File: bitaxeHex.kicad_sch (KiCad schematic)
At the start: 26 parts, among them J1 Screw Terminal, J2 Screw Terminal

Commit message: minor update
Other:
- sheet BM1366-1 renamed BM1368-1
- sheet BM1366-2 renamed BM1368-2
- sheet BM1366-3 renamed BM1368-3
- sheet ESP32 ports: added 1V2_IO; removed 1V8_IO
- sheet Power ports: added 1V2_IO; removed 1V8_IO
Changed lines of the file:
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@@
 		)
 	)
-	(label "1V8"
+	(label "1V2"
 		(at 50.165 88.265 0)
 		(fields_autoplaced yes)
@@
 		)
 	)
-	(label "1V8"
+	(label "1V2"
 		(at 86.995 36.195 180)
 		(fields_autoplaced yes)
@@
 			(color 255 255 194 1.0000)
 		)
-		(property "Sheetname" "BM1366-1"
+		(property "Sheetname" "BM1368-1"
 			(at 127.635 73.66 0)
 			(effects
@@
 			(color 255 255 194 1.0000)
 		)
-		(property "Sheetname" "BM1366-2"
+		(property "Sheetname" "BM1368-2"
 			(at 165.1 73.66 0)
 			(effects
@@
 			)
 		)
-		(pin "1V8_IO" output
+		(pin "1V2_IO" output
 			(at 79.375 36.195 0)
 			(effects
@@
 			)
 		)
-		(pin "1V8_IO" input
+		(pin "1V2_IO" input
 			(at 59.69 88.265 180)
 			(effects
@@
 			(color 255 255 194 1.0000)
 		)
-		(property "Sheetname" "BM1366-3"
+		(property "Sheetname" "BM1368-3"
 			(at 203.835 73.66 0)
 			(effects

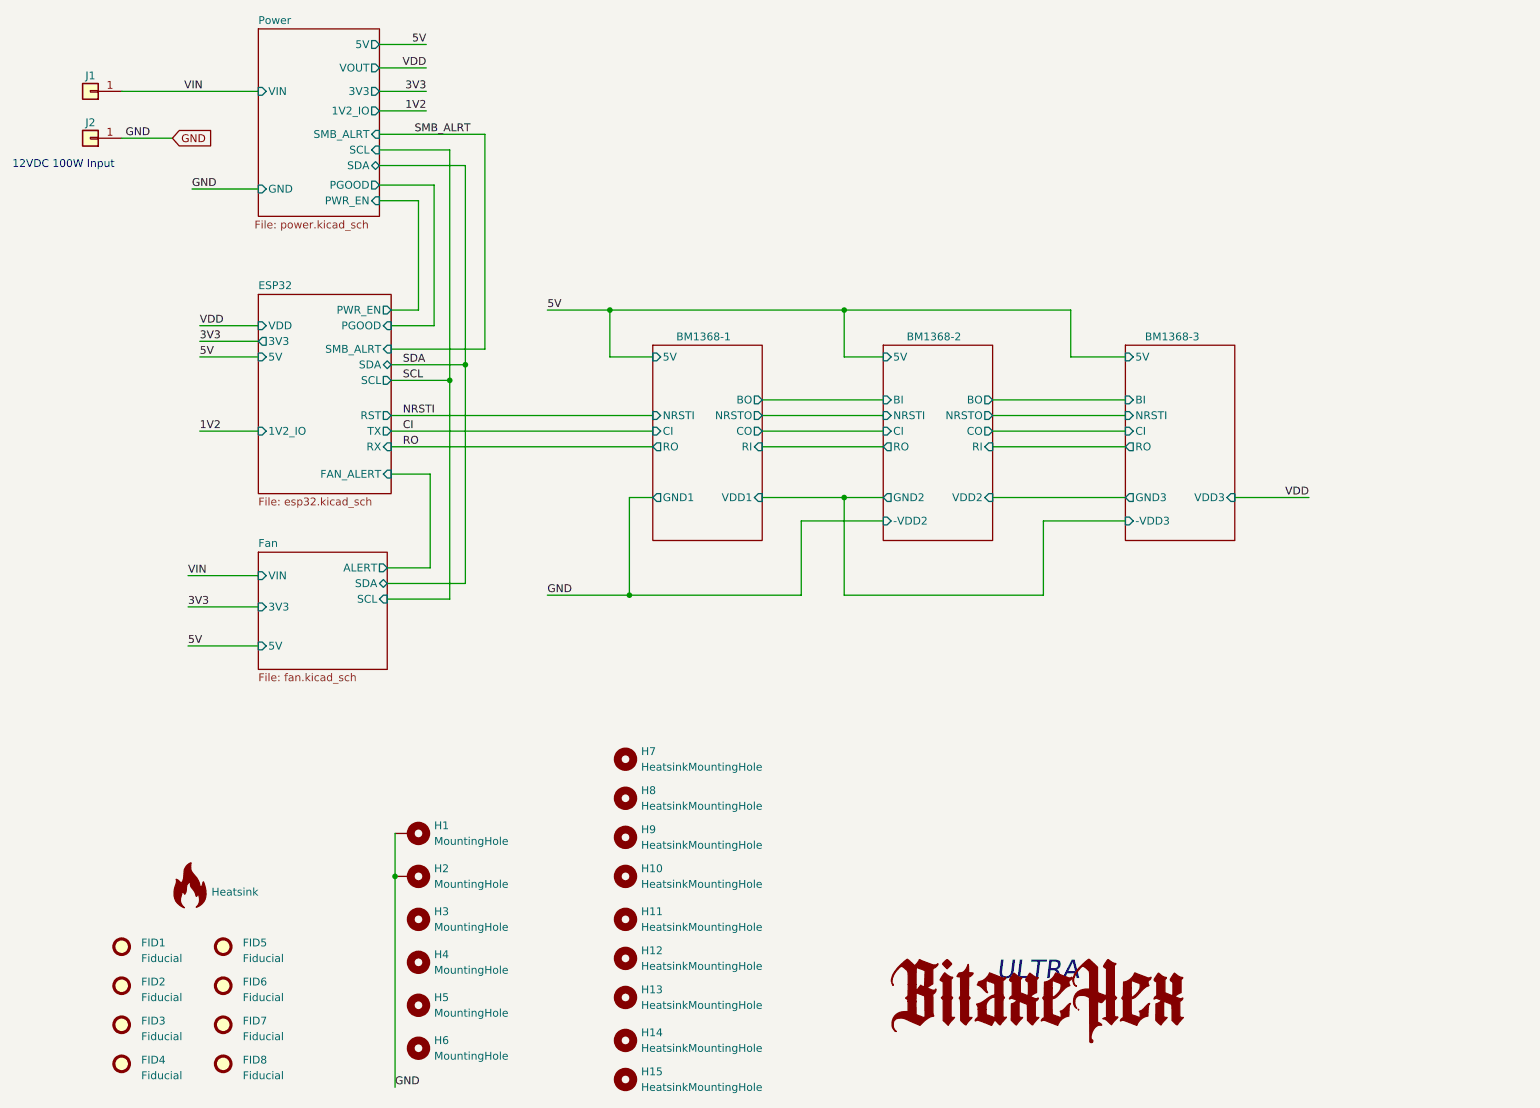
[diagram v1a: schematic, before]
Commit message: Adding temperature monitoring
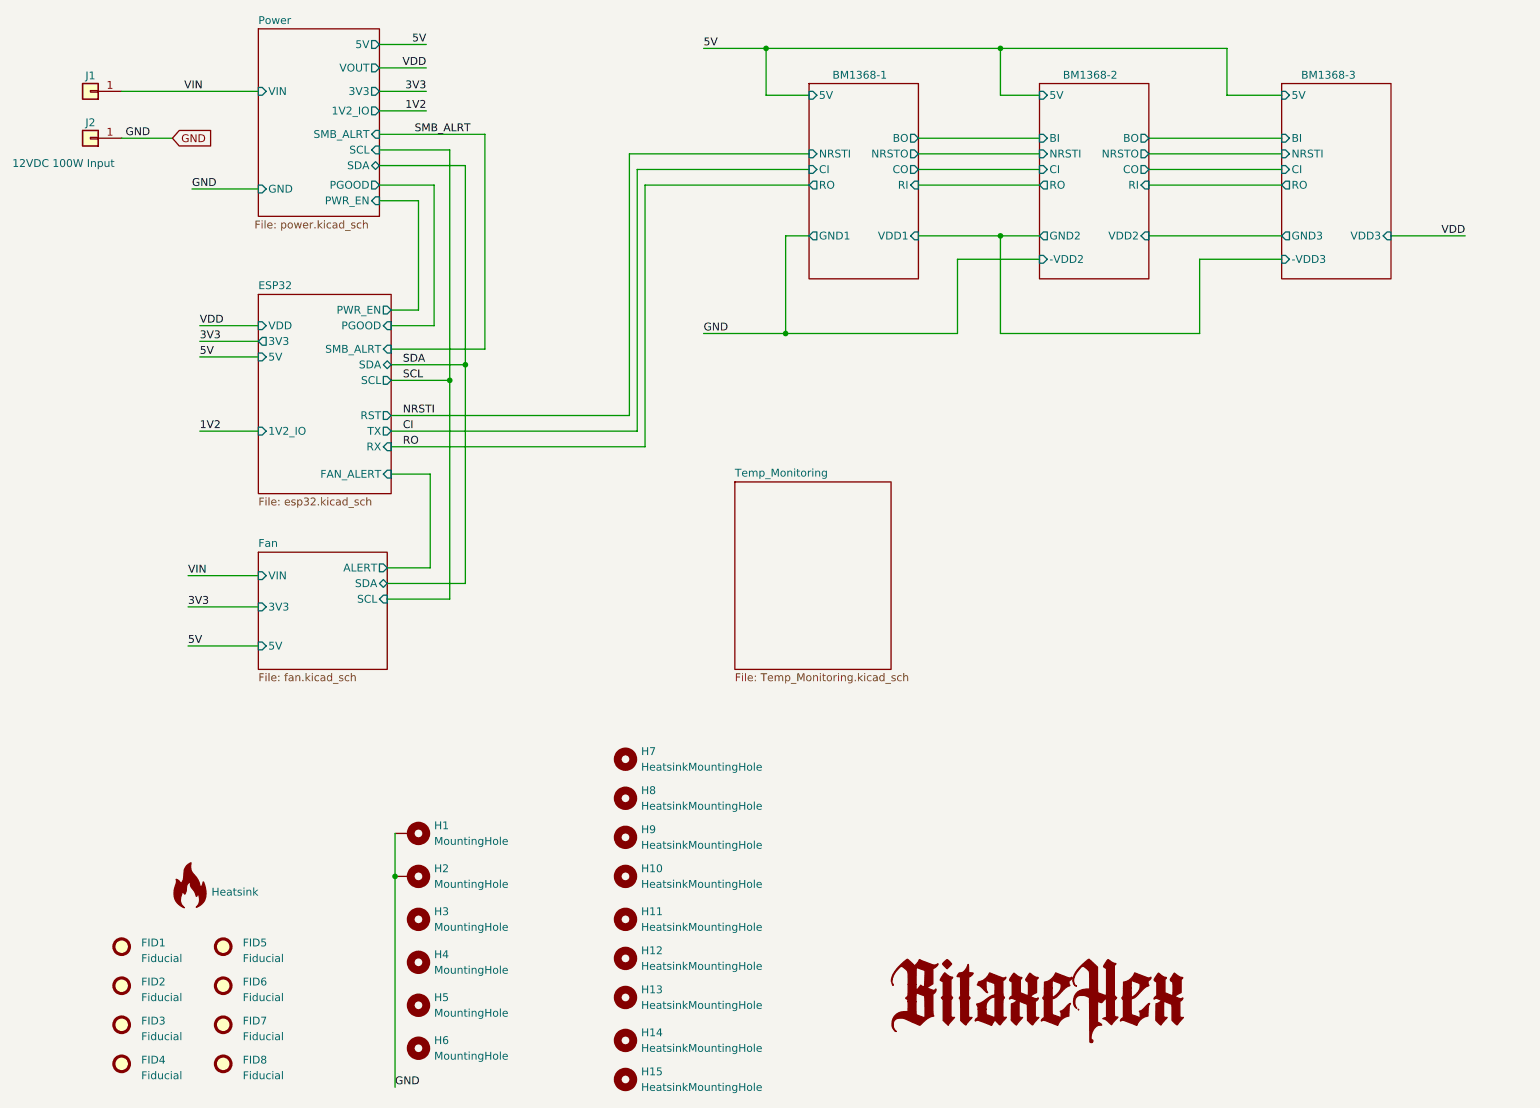
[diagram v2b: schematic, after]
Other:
- added sheet Temp_Monitoring (Temp_Monitoring.kicad_sch)
- note removed: "ULTRA"

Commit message: sch update done
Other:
- sheet BM1368-1 ports: added TEMP_N1, TEMP_N2, TEMP_P1, TEMP_P2; removed none
- sheet BM1368-2 ports: added TEMP_N3, TEMP_N4, TEMP_P3, TEMP_P4; removed none
- sheet BM1368-3 ports: added TEMP_N5, TEMP_N6, TEMP_P5, TEMP_P6; removed none
- sheet ESP32 ports: added ALERT_TEMP, OVERT_TEMP; removed none
- sheet Temp_Monitoring ports: added 3V3, ALERT_TEMP, OVERT_TEMP, SCL, SDA, TEMP_N1, TEMP_N2, TEMP_N3, TEMP_N4, TEMP_N5, TEMP_N6, TEMP_P1, TEMP_P2, TEMP_P3, TEMP_P4, TEMP_P5, TEMP_P6; removed none

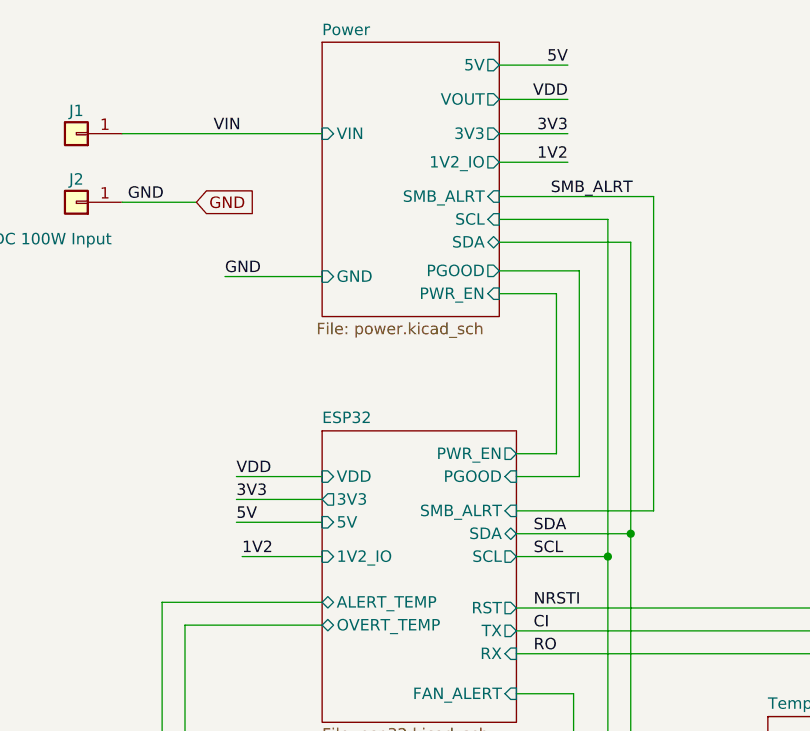
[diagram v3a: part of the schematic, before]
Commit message: Reset to 1V8
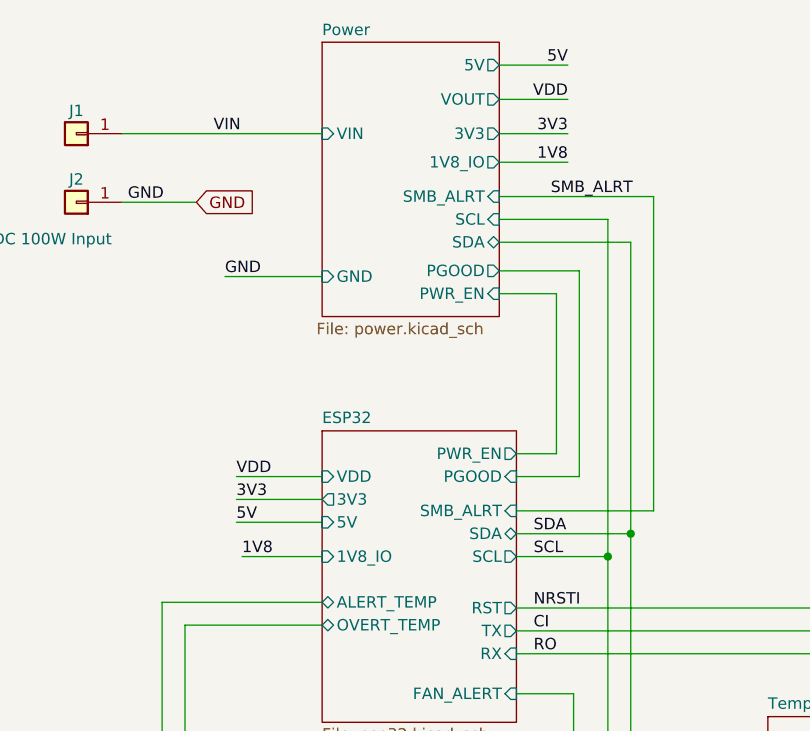
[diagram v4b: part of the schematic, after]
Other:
- sheet ESP32 ports: added 1V8_IO; removed 1V2_IO
- sheet Power ports: added 1V8_IO; removed 1V2_IO
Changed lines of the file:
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@@
 		)
 	)
-	(label "1V2"
+	(label "1V8"
 		(at 50.8 80.01 0)
 		(fields_autoplaced yes)
@@
 		)
 	)
-	(label "1V2"
+	(label "1V8"
 		(at 86.995 36.195 180)
 		(fields_autoplaced yes)
@@
 			)
 		)
-		(pin "1V2_IO" output
+		(pin "1V8_IO" output
 			(at 79.375 36.195 0)
 			(effects
@@
 			)
 		)
-		(pin "1V2_IO" input
+		(pin "1V8_IO" input
 			(at 59.69 80.01 180)
 			(effects

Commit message: init push for GammaHex
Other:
- sheet BM1368-1 renamed BM1370-1
- sheet BM1368-2 renamed BM1370-2
- sheet BM1368-3 renamed BM1370-3
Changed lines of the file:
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@@
 			(color 255 255 194 1.0000)
 		)
-		(property "Sheetname" "BM1368-1"
+		(property "Sheetname" "BM1370-1"
 			(at 163.195 31.115 0)
 			(effects
@@
 			(color 255 255 194 1.0000)
 		)
-		(property "Sheetname" "BM1368-2"
+		(property "Sheetname" "BM1370-2"
 			(at 200.66 31.115 0)
 			(effects
@@
 			(color 255 255 194 1.0000)
 		)
-		(property "Sheetname" "BM1368-3"
+		(property "Sheetname" "BM1370-3"
 			(at 239.395 31.115 0)
 			(effects
